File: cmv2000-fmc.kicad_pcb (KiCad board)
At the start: 4 copper layers, 70 x 35 mm, 75 parts, among them J1 Conn_01x02, J10 LVDS_CTR_P, J11 LVDS_CTR_N, J12 LVDS_1_P, J13 LVDS_1_N, J14 LVDS_2_P, J15 LVDS_2_N, J2 Conn_02x05, J3 LVDS_CLK_IN_P, J4 LVDS_CLK_IN_N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

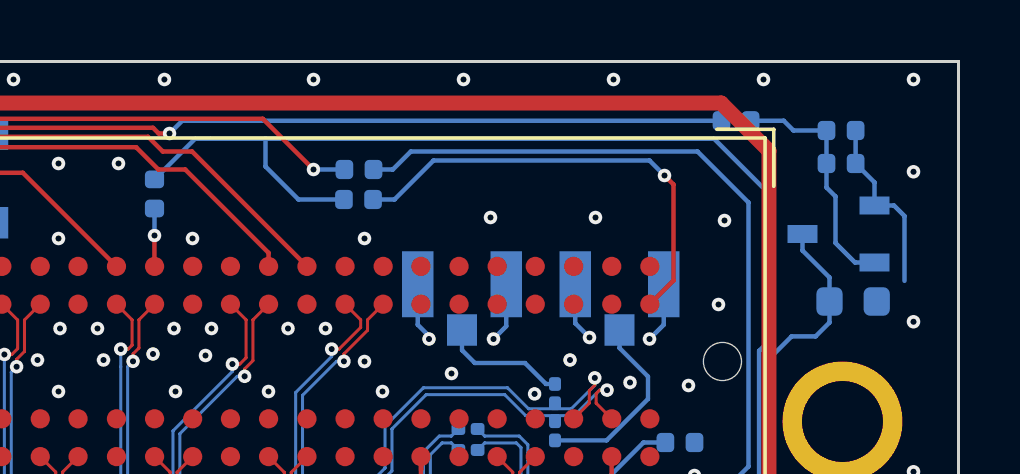
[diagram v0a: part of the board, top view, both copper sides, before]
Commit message: use R27 and R28 as voltage divider at voltage detector (U3) output
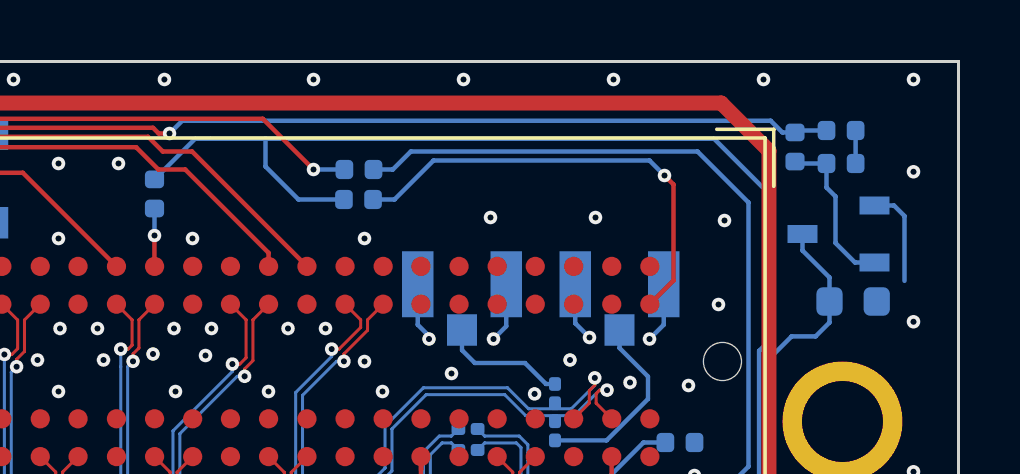
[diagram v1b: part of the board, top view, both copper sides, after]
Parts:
- R27: value 100k -> 33k
- R28: value 1k -> 10k
- moved R28 2.15 mm to (177.1, 87.8), turned to 270 degrees
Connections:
- R27 pad 1: Net-(C8-Pad1) -> /CAM_PWR_GOOD
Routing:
- net /CAM_PWR_GOOD: track 82.5 -> 86.2 mm
- net Net-(C8-Pad1): track 8.11 -> 5.42 mm
- net GND: track 166.3 -> 164.6 mm
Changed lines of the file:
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@@
     (add_net "Net-(D3-Pad2)")
     (add_net "Net-(JP1-Pad1)")
-    (add_net "Net-(P1-PadC02)")
-    (add_net "Net-(P1-PadC03)")
-    (add_net "Net-(P1-PadC06)")
-    (add_net "Net-(P1-PadC07)")
     (add_net "Net-(P1-PadC14)")
     (add_net "Net-(P1-PadC30)")
     (add_net "Net-(P1-PadC31)")
-    (add_net "Net-(P1-PadC34)")
-    (add_net "Net-(P1-PadC39)")
     (add_net "Net-(P1-PadD01)")
-    (add_net "Net-(P1-PadD04)")
-    (add_net "Net-(P1-PadD05)")
-    (add_net "Net-(P1-PadD29)")
     (add_net "Net-(P1-PadD30)")
     (add_net "Net-(P1-PadD31)")
-    (add_net "Net-(P1-PadD32)")
-    (add_net "Net-(P1-PadD33)")
-    (add_net "Net-(P1-PadD34)")
-    (add_net "Net-(P1-PadD35)")
-    (add_net "Net-(P1-PadG06)")
-    (add_net "Net-(P1-PadG07)")
-    (add_net "Net-(P1-PadG09)")
-    (add_net "Net-(P1-PadG10)")
-    (add_net "Net-(P1-PadG12)")
-    (add_net "Net-(P1-PadG13)")
-    (add_net "Net-(P1-PadG15)")
-    (add_net "Net-(P1-PadG16)")
-    (add_net "Net-(P1-PadG18)")
-    (add_net "Net-(P1-PadG19)")
-    (add_net "Net-(P1-PadG21)")
-    (add_net "Net-(P1-PadG22)")
-    (add_net "Net-(P1-PadG24)")
-    (add_net "Net-(P1-PadG25)")
-    (add_net "Net-(P1-PadG27)")
-    (add_net "Net-(P1-PadG28)")
-    (add_net "Net-(P1-PadG30)")
-    (add_net "Net-(P1-PadG31)")
-    (add_net "Net-(P1-PadG33)")
-    (add_net "Net-(P1-PadG34)")
-    (add_net "Net-(P1-PadG36)")
-    (add_net "Net-(P1-PadG37)")
-    (add_net "Net-(P1-PadH01)")
     (add_net "Net-(P1-PadH02)")
     (add_net "Net-(P1-PadH07)")
-    (add_net "Net-(P1-PadH08)")
-    (add_net "Net-(P1-PadH40)")
-    (add_net "Net-(P2-Pad1)")
-    (add_net "Net-(P2-Pad10)")
-    (add_net "Net-(P2-Pad11)")
-    (add_net "Net-(P2-Pad12)")
-    (add_net "Net-(P2-Pad13)")
-    (add_net "Net-(P2-Pad14)")
-    (add_net "Net-(P2-Pad2)")
-    (add_net "Net-(P2-Pad3)")
-    (add_net "Net-(P2-Pad4)")
-    (add_net "Net-(P2-Pad5)")
-    (add_net "Net-(P2-Pad6)")
-    (add_net "Net-(P2-Pad7)")
-    (add_net "Net-(P2-Pad8)")
-    (add_net "Net-(P2-Pad9)")
     (add_net "Net-(Q1-Pad3)")
     (add_net "Net-(R10-Pad1)")
@@
     (tags capacitor)
     (attr smd)
-    (fp_text reference C8 (at -1.935 0) (layer B.SilkS)
+    (fp_text reference C8 (at 1.565 0 90) (layer B.SilkS)
       (effects (font (size 0.8 0.8) (thickness 0.15)) (justify mirror))
     )
@@
       (effects (font (size 0.8 0.8) (thickness 0.15)) (justify mirror))
     )
-    (fp_text value 100k (at 0 -1.17) (layer B.Fab)
+    (fp_text value 33k (at 0 -1.17) (layer B.Fab)
       (effects (font (size 1 1) (thickness 0.15)) (justify mirror))
     )
@@
       (net 2 GND))
     (pad 1 smd roundrect (at -0.485 0) (size 0.59 0.64) (layers B.Cu B.Paste B.Mask) (roundrect_rratio 0.25)
-      (net 89 "Net-(C8-Pad1)"))
+      (net 90 /CAM_PWR_GOOD))
     (model ${KISYS3DMOD}/Resistor_SMD.3dshapes/R_0402_1005Metric.wrl
       (at (xyz 0 0 0))
@@
   )
   (module Resistor_SMD:R_0402_1005Metric (layer B.Cu)
-    (at 175.085 86.975)
+    (at 177.05 87.85 270)
     (descr "Resistor SMD 0402 (1005 Metric), square (rectangular) end terminal, IPC_7351 nominal, (Body size source: http://www.tortai-tech.com/upload/download/2011102023233369053.pdf), generated with kicad-footprint-generator")
     (tags resistor)
     (attr smd)
-    (fp_text reference R28 (at -2.535 0.025) (layer B.SilkS)
+    (fp_text reference R28 (at 0 1.1 90) (layer B.SilkS)
       (effects (font (size 0.8 0.8) (thickness 0.15)) (justify mirror))
     )
-    (fp_text value 1k (at 0 -1.17) (layer B.Fab)
+    (fp_text value 10k (at 0 -1.17 90) (layer B.Fab)
       (effects (font (size 1 1) (thickness 0.15)) (justify mirror))
     )
-    (fp_text user %R (at 0 0) (layer B.Fab)
+    (fp_text user %R (at 0 0 90) (layer B.Fab)
       (effects (font (size 0.25 0.25) (thickness 0.04)) (justify mirror))
     )
@@
     (fp_line (start -0.5 0.25) (end 0.5 0.25) (layer B.Fab) (width 0.1))
     (fp_line (start -0.5 -0.25) (end -0.5 0.25) (layer B.Fab) (width 0.1))
-    (pad 2 smd roundrect (at 0.485 0) (size 0.59 0.64) (layers B.Cu B.Paste B.Mask) (roundrect_rratio 0.25)
+    (pad 2 smd roundrect (at 0.485 0 270) (size 0.59 0.64) (layers B.Cu B.Paste B.Mask) (roundrect_rratio 0.25)
       (net 89 "Net-(C8-Pad1)"))
-    (pad 1 smd roundrect (at -0.485 0) (size 0.59 0.64) (layers B.Cu B.Paste B.Mask) (roundrect_rratio 0.25)
+    (pad 1 smd roundrect (at -0.485 0 270) (size 0.59 0.64) (layers B.Cu B.Paste B.Mask) (roundrect_rratio 0.25)
       (net 90 /CAM_PWR_GOOD))
     (model ${KISYS3DMOD}/Resistor_SMD.3dshapes/R_0402_1005Metric.wrl
@@
   (segment (start 180.35 89.8) (end 180.7 90.15) (width 0.15) (layer B.Cu) (net 2))
   (segment (start 179.07 87.3) (end 179.07 88.4) (width 0.15) (layer B.Cu) (net 2))
-  (segment (start 179.7 89.03) (end 179.07 88.4) (width 0.15) (layer B.Cu) (net 2))
-  (segment (start 179.7 89.8) (end 179.7 89.03) (width 0.15) (layer B.Cu) (net 2))
   (segment (start 133.4 94.825) (end 132.775 94.825) (width 0.15) (layer B.Cu) (net 2))
   (segment (start 132.775 94.825) (end 132.1 95.5) (width 0.15) (layer B.Cu) (net 2))
@@
   (segment (start 178.1 89.2) (end 178.1 88.4) (width 0.15) (layer B.Cu) (net 89))
   (segment (start 178.4 89.5) (end 178.1 89.2) (width 0.15) (layer B.Cu) (net 89))
-  (segment (start 178.1 88.4) (end 178.1 87.3) (width 0.15) (layer B.Cu) (net 89))
-  (segment (start 178.1 87.3) (end 177 87.3) (width 0.15) (layer B.Cu) (net 89))
-  (segment (start 176.675 86.975) (end 175.57 86.975) (width 0.15) (layer B.Cu) (net 89))
-  (segment (start 177 87.3) (end 176.675 86.975) (width 0.15) (layer B.Cu) (net 89))
+  (segment (start 177.115 88.4) (end 177.05 88.335) (width 0.15) (layer B.Cu) (net 89))
+  (segment (start 178.1 88.4) (end 177.115 88.4) (width 0.15) (layer B.Cu) (net 89))
   (segment (start 132.025 94.775) (end 130.7 94.775) (width 0.15) (layer B.Cu) (net 90))
   (via (at 130.4 95.075) (size 0.45) (drill 0.2) (layers F.Cu B.Cu) (net 90))
@@
   (segment (start 133.525 93.525) (end 133.4 93.525) (width 0.15) (layer B.Cu) (net 90))
   (via (at 156.2 87.4) (size 0.45) (drill 0.2) (layers F.Cu B.Cu) (net 90))
-  (segment (start 156.625 86.975) (end 156.2 87.4) (width 0.15) (layer B.Cu) (net 90))
-  (segment (start 174.6 86.975) (end 156.625 86.975) (width 0.15) (layer B.Cu) (net 90))
   (via (at 123.199999 87.199999) (size 0.45) (drill 0.2) (layers F.Cu B.Cu) (net 90))
   (segment (start 124.915008 87.589537) (end 124.048747 87.589537) (width 0.15) (layer F.Cu) (net 90))
@@
   (segment (start 123.199999 87.199999) (end 122.946 86.946) (width 0.15) (layer B.Cu) (net 90))
   (segment (start 122.946 86.946) (end 119.304 86.946) (width 0.15) (layer B.Cu) (net 90))
+  (segment (start 177.115 87.3) (end 177.05 87.365) (width 0.15) (layer B.Cu) (net 90))
+  (segment (start 178.1 87.3) (end 177.115 87.3) (width 0.15) (layer B.Cu) (net 90))
+  (segment (start 156.625 86.975) (end 156.2 87.4) (width 0.15) (layer B.Cu) (net 90))
+  (segment (start 176.24 86.975) (end 156.625 86.975) (width 0.15) (layer B.Cu) (net 90))
+  (segment (start 176.63 87.365) (end 176.24 86.975) (width 0.15) (layer B.Cu) (net 90))
+  (segment (start 177.05 87.365) (end 176.63 87.365) (width 0.15) (layer B.Cu) (net 90))
   (segment (start 126.35 97.455) (end 126.35 96.375) (width 0.15) (layer B.Cu) (net 91))
   (segment (start 126.7 97.805) (end 126.35 97.455) (width 0.15) (layer B.Cu) (net 91))

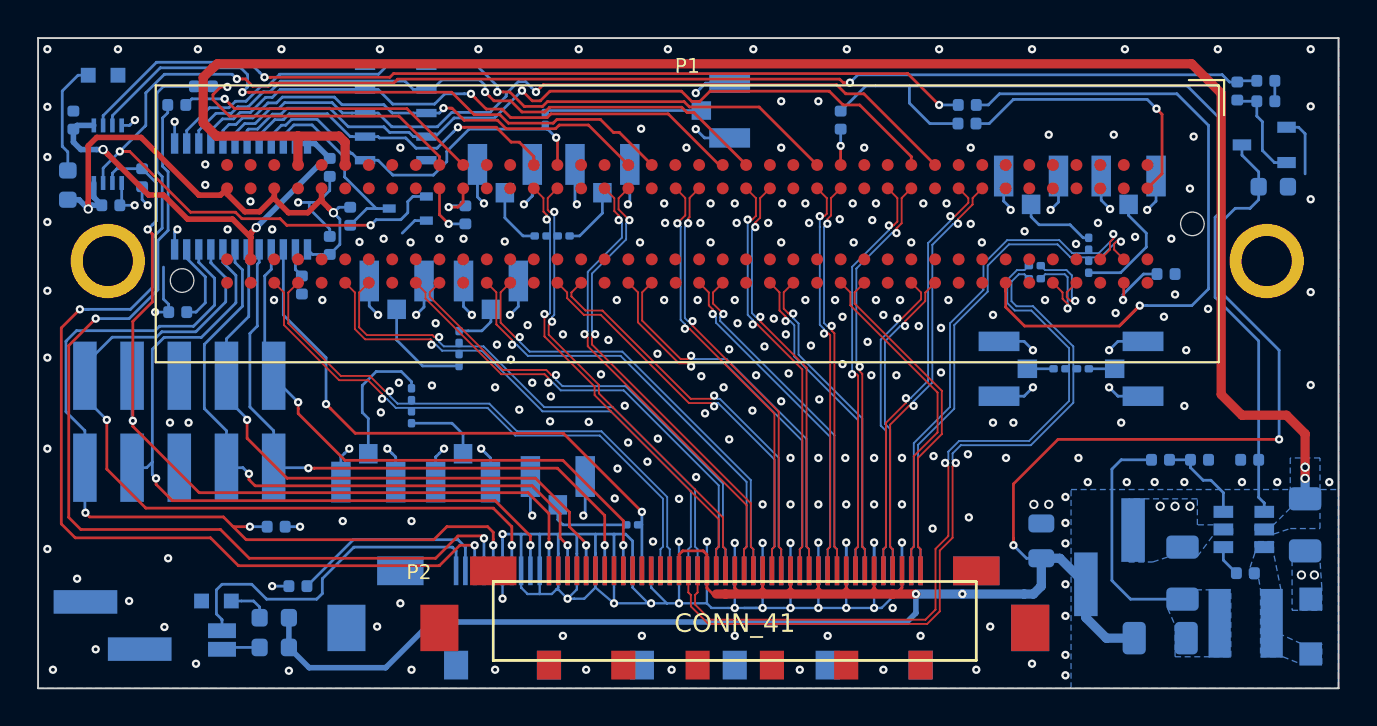
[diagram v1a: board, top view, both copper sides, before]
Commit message: add optional bootstrap diode, as recommended by AP3211 appnote
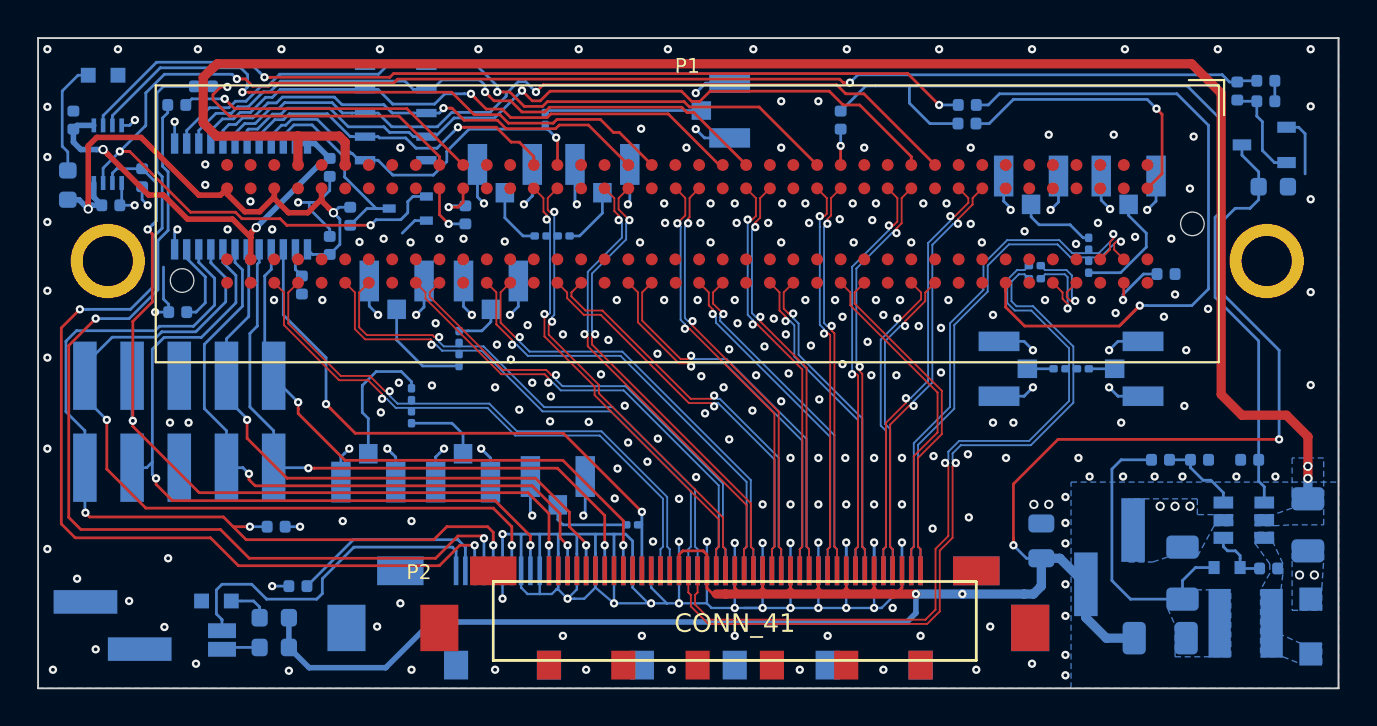
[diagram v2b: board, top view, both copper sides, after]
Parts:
- added D4: D, Diode_SMD:D_SOD-523, B.Cu at (176.5, 113.5)
- moved C3 1.27 mm to (178.7, 113.5)
- moved U1 0.50 mm to (177.4, 111.0)
- moved C1 0.15 mm to (180.8, 111.2)
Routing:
- net Net-(C4-Pad1): track 12.6 -> 15.5 mm
- net Net-(C3-Pad1): track 1.69 -> 3.29 mm
- net /CAM_PWR_ON: track 48.1 -> 47.6 mm
- net Net-(R10-Pad1): track 4.91 -> 4.41 mm
- net GND: vias 271 -> 270

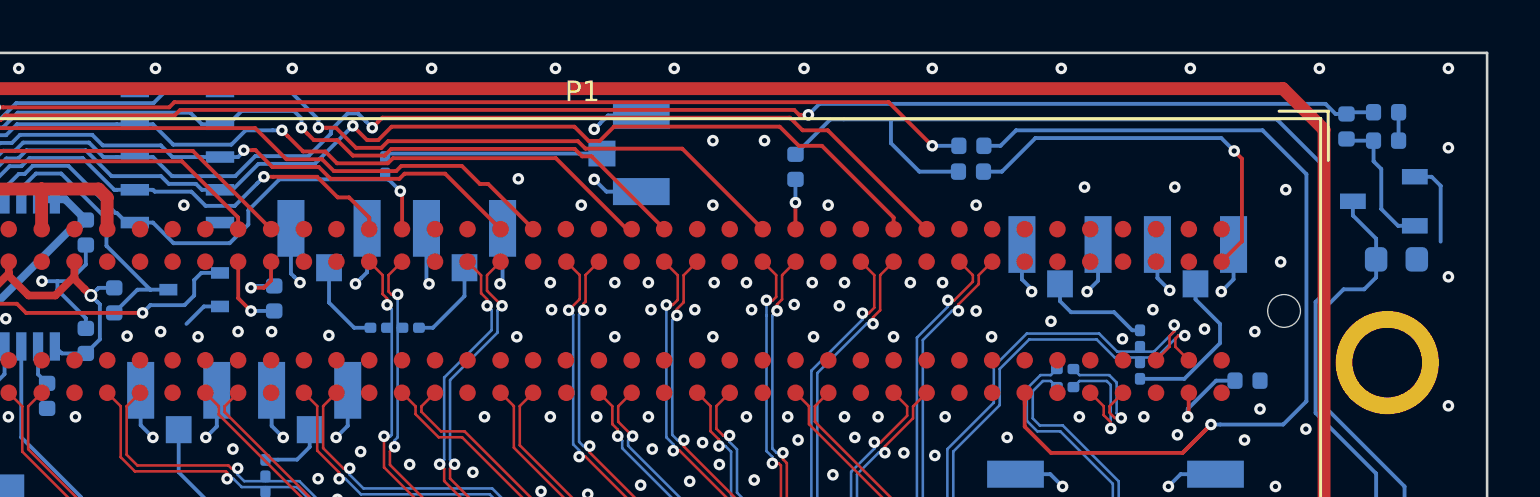
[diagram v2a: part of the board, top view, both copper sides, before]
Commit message: fix two courtyard DRC problems
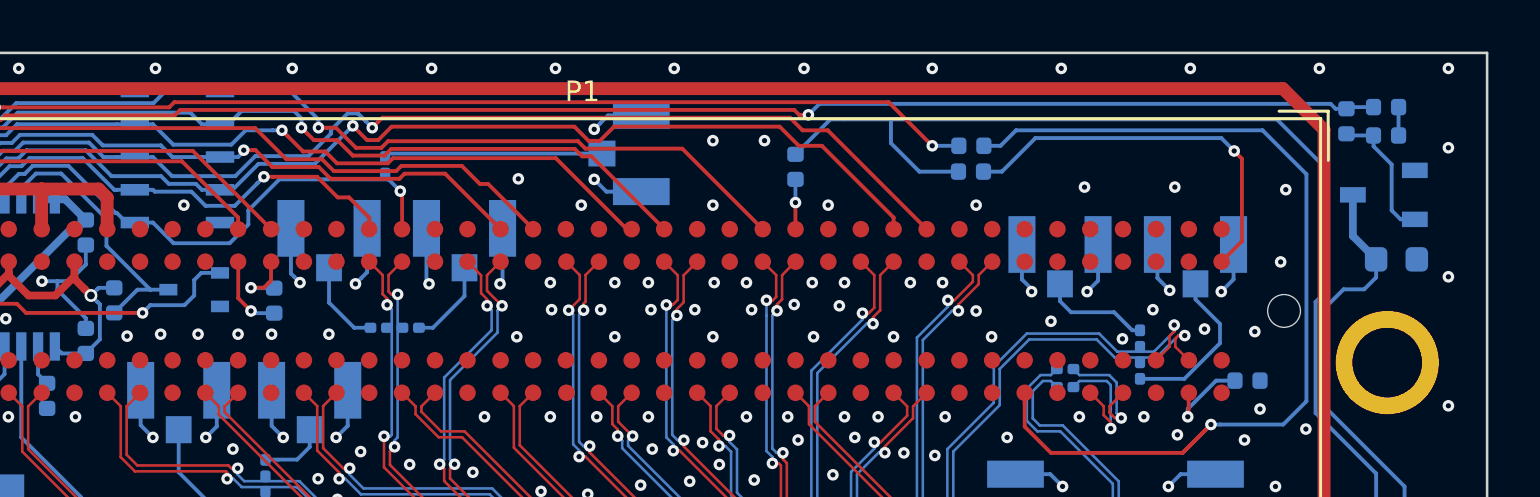
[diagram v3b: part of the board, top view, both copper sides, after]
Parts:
- moved U3 0.25 mm to (178.5, 90.5)
- moved C8 0.20 mm to (178.6, 88.2)
- moved R27 0.20 mm to (178.6, 87.1)
- moved R28 0.20 mm to (177.1, 87.7)
- moved R12 0.08 mm to (135.5, 94.6)
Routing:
- net GND: track 164.6 -> 159.7 mm
